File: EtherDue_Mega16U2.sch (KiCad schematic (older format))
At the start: 26 parts, among them IC501 ATMEGA16U2, P501 USB_5PIN_SHELL, U501 74LVC1G125, X501 12MHz KX-7 20pF

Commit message: Remove 74LVC1G125 buffer used for level translation on 16U2 TX pin, replace with resistor divider
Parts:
- removed C504: 100nF, symbol C
- removed U501: 74LVC1G125, symbol 74LVC1G125
- added R509: 1K5, symbol R
- added R510: 2K7, symbol R
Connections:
- net labels removed: +3.3V
- wire segments 106 -> 101

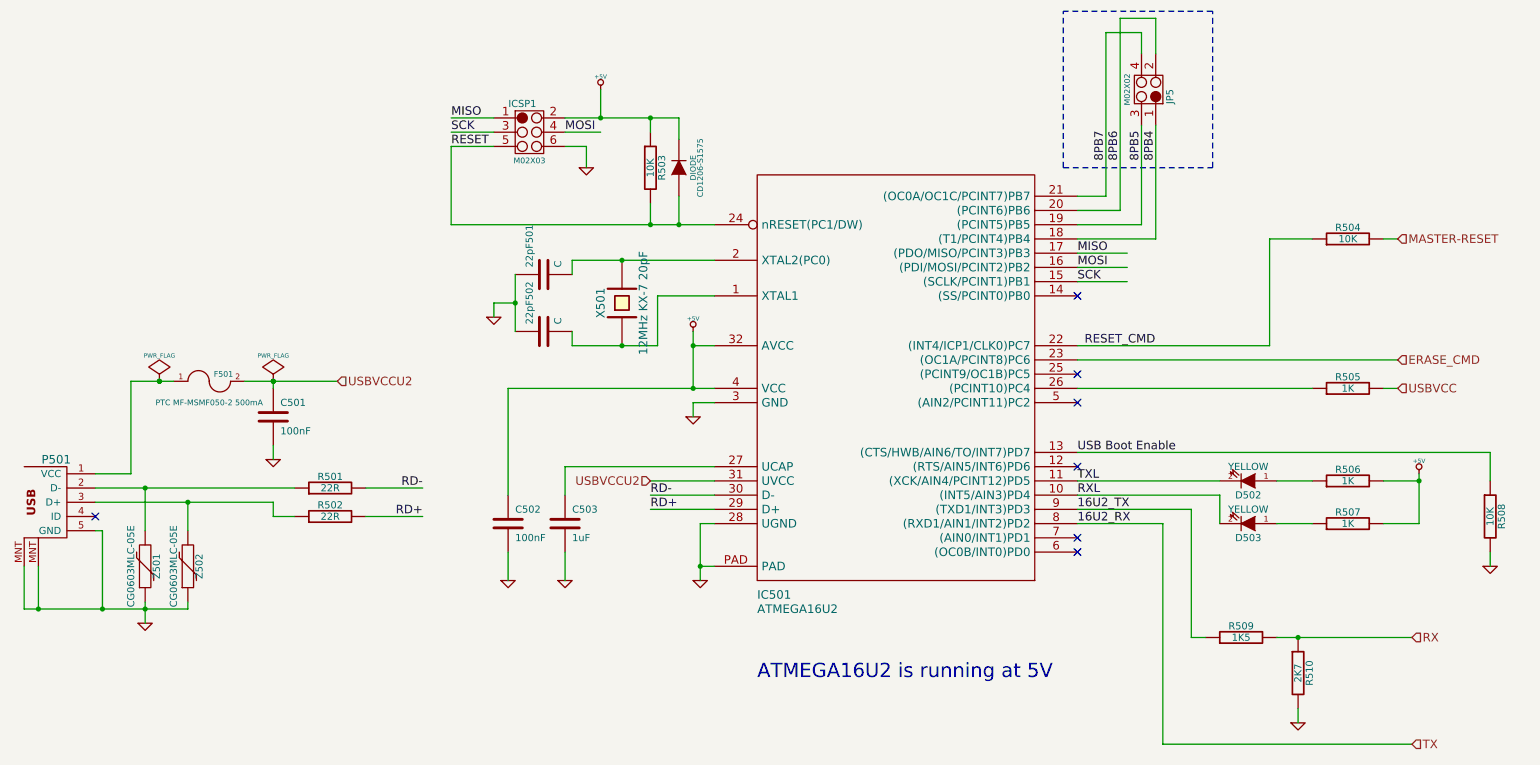
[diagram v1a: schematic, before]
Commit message: Add W5100 Ethernet components
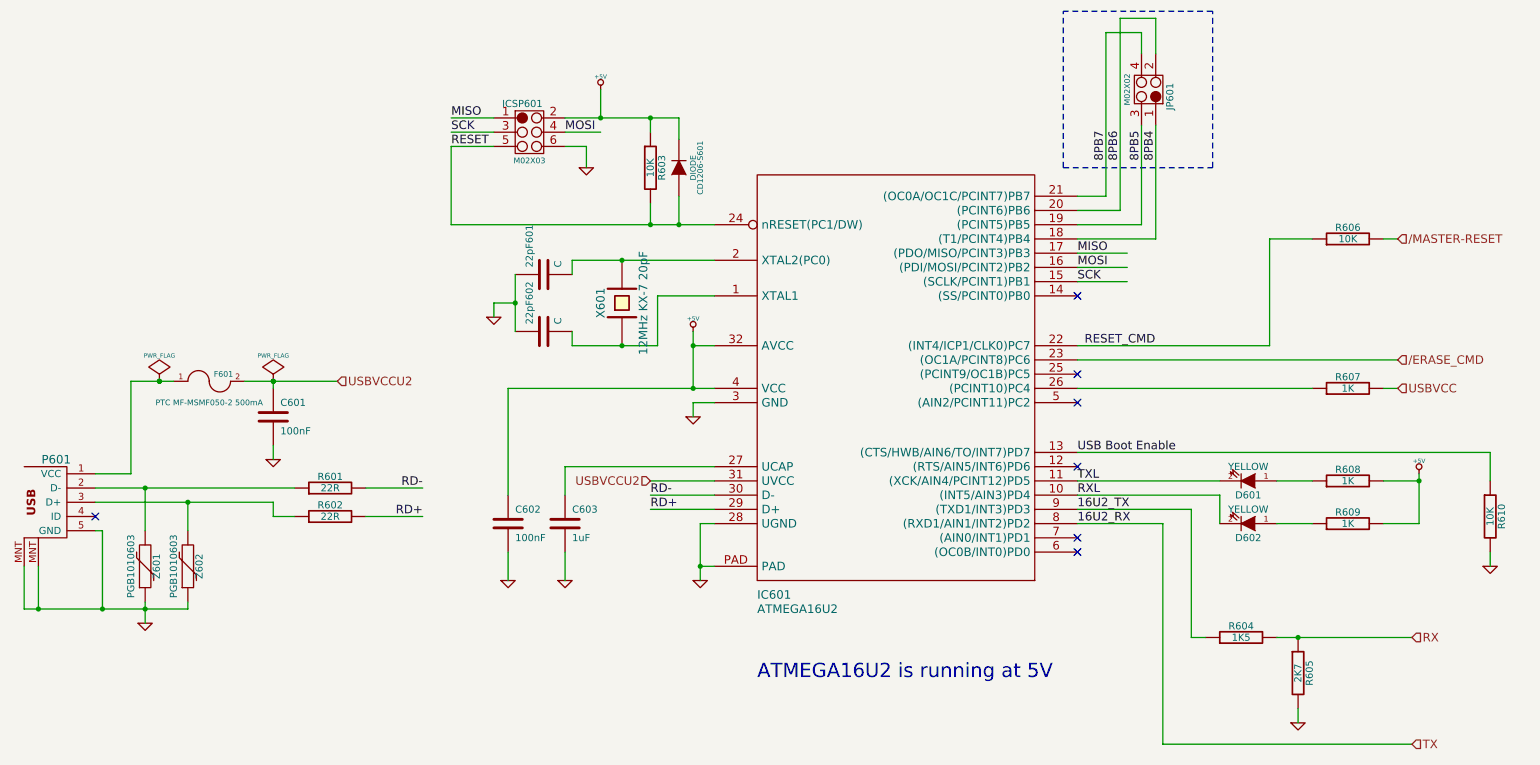
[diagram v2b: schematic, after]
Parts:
- Z601: renamed from Z501; value CG0603MLC-05E -> PGB1010603
- Z602: renamed from Z502; value CG0603MLC-05E -> PGB1010603
- renumbered 22pF501 to 22pF601, 22pF502 to 22pF602, C501 to C601, C502 to C602, C503 to C603, CD1206-S1575 to CD1206-S601, D502 to D601, D503 to D602, F501 to F601, IC501 to IC601, ICSP1 to ICSP601, JP5 to JP601, P501 to P601, R501 to R601, R502 to R602, R503 to R603, R509 to R604, R510 to R605, R504 to R606, R505 to R607, R506 to R608, R507 to R609, R508 to R610, X501 to X601
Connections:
- net labels added: /ERASE_CMD, /MASTER-RESET
- net labels removed: ERASE_CMD, MASTER-RESET
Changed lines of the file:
@@
-EESchema Schematic File Version 2  date Wed 10 Apr 2013 15:09:30 EST
+EESchema Schematic File Version 2  date Thu 11 Apr 2013 15:03:05 EST
 LIBS:power
 LIBS:device
@@
 $Descr A4 11700 8267
 encoding utf-8
-Sheet 5 5
+Sheet 6 6
 Title ""
-Date "10 apr 2013"
+Date "11 apr 2013"
 Rev ""
 Comp ""
@@
 	9650 5800 9650 5900
 $Comp
-L GND #PWR511
+L GND #PWR092
 U 1 1 5164F3D5
 P 9650 5900
-F 0 "#PWR511" H 9650 5900 30  0001 C CNN
+F 0 "#PWR092" H 9650 5900 30  0001 C CNN
 F 1 "GND" H 9650 5830 30  0001 C CNN
 	1    9650 5900
@@
 $EndComp
 $Comp
-L R R510
+L R R605
 U 1 1 5164F3AD
 P 9650 5550
-F 0 "R510" V 9730 5550 50  0000 C CNN
+F 0 "R605" V 9730 5550 50  0000 C CNN
 F 1 "2K7" V 9650 5550 50  0000 C CNN
 	1    9650 5550
@@
 $EndComp
 $Comp
-L R R509
+L R R604
 U 1 1 5164F3A2
 P 9250 5300
-F 0 "R509" V 9330 5300 50  0000 C CNN
+F 0 "R604" V 9330 5300 50  0000 C CNN
 F 1 "1K5" V 9250 5300 50  0000 C CNN
 	1    9250 5300
@@
 $EndComp
 $Comp
-L PWR_FLAG #FLG502
+L PWR_FLAG #FLG093
 U 1 1 5163B502
 P 2450 3500
-F 0 "#FLG502" H 2450 3595 30  0001 C CNN
+F 0 "#FLG093" H 2450 3595 30  0001 C CNN
 F 1 "PWR_FLAG" H 2450 3680 30  0000 C CNN
 	1    2450 3500
@@
 $EndComp
 $Comp
-L PWR_FLAG #FLG501
+L PWR_FLAG #FLG094
 U 1 1 5163B4F2
 P 1650 3500
-F 0 "#FLG501" H 1650 3595 30  0001 C CNN
+F 0 "#FLG094" H 1650 3595 30  0001 C CNN
 F 1 "PWR_FLAG" H 1650 3680 30  0000 C CNN
 	1    1650 3500
@@
 USBVCC
 Text HLabel 10350 3350 2    60   Input ~ 0
-ERASE_CMD
+/ERASE_CMD
 Text HLabel 10350 2500 2    60   Input ~ 0
-MASTER-RESET
+/MASTER-RESET
 Text HLabel 5100 4200 0    60   Input ~ 0
 USBVCCU2
@@
 TXL
 $Comp
-L +5V #PWR512
+L +5V #PWR095
 U 1 1 515BD66E
 P 10500 4150
-F 0 "#PWR512" H 10500 4240 20  0001 C CNN
+F 0 "#PWR095" H 10500 4240 20  0001 C CNN
 F 1 "+5V" H 10500 4240 30  0000 C CNN
 	1    10500 4150
@@
 $EndComp
 $Comp
-L R R506
+L R R608
 U 1 1 515BD664
 P 10000 4200
-F 0 "R506" V 10080 4200 50  0000 C CNN
+F 0 "R608" V 10080 4200 50  0000 C CNN
 F 1 "1K" V 10000 4200 50  0000 C CNN
 	1    10000 4200
@@
 $EndComp
 $Comp
-L R R507
+L R R609
 U 1 1 515BD654
 P 10000 4500
-F 0 "R507" V 10080 4500 50  0000 C CNN
+F 0 "R609" V 10080 4500 50  0000 C CNN
 F 1 "1K" V 10000 4500 50  0000 C CNN
 	1    10000 4500
@@
 $EndComp
 $Comp
-L LED D503
+L LED D602
 U 1 1 515BD64B
 P 9300 4500
-F 0 "D503" H 9300 4600 50  0000 C CNN
+F 0 "D602" H 9300 4600 50  0000 C CNN
 F 1 "YELLOW" H 9300 4400 50  0000 C CNN
 	1    9300 4500
@@
 $EndComp
 $Comp
-L LED D502
+L LED D601
 U 1 1 515BD62A
 P 9300 4200
-F 0 "D502" H 9300 4300 50  0000 C CNN
+F 0 "D601" H 9300 4300 50  0000 C CNN
 F 1 "YELLOW" H 9300 4100 50  0000 C CNN
 	1    9300 4200
@@
 NoConn ~ 8100 4100
 $Comp
-L GND #PWR513
+L GND #PWR096
 U 1 1 515BD60A
 P 11000 4800
-F 0 "#PWR513" H 11000 4800 30  0001 C CNN
+F 0 "#PWR096" H 11000 4800 30  0001 C CNN
 F 1 "GND" H 11000 4730 30  0001 C CNN
 	1    11000 4800
@@
 $EndComp
 $Comp
-L R R508
+L R R610
 U 1 1 515BD5FC
 P 11000 4450
-F 0 "R508" V 11080 4450 50  0000 C CNN
+F 0 "R610" V 11080 4450 50  0000 C CNN
 F 1 "10K" V 11000 4450 50  0000 C CNN
 	1    11000 4450
@@
 NoConn ~ 8100 3650
 $Comp
-L R R505
+L R R607
 U 1 1 515BD5C8
 P 10000 3550
-F 0 "R505" V 10080 3550 50  0000 C CNN
+F 0 "R607" V 10080 3550 50  0000 C CNN
 F 1 "1K" V 10000 3550 50  0000 C CNN
 	1    10000 3550
@@
 RESET_CMD
 $Comp
-L R R504
+L R R606
 U 1 1 515BD538
 P 10000 2500
-F 0 "R504" V 10080 2500 50  0000 C CNN
+F 0 "R606" V 10080 2500 50  0000 C CNN
 F 1 "10K" V 10000 2500 50  0000 C CNN
 	1    10000 2500
@@
 RD-
 $Comp
-L R R502
+L R R602
 U 1 1 515BD4B0
 P 2850 4450
-F 0 "R502" V 2930 4450 50  0000 C CNN
+F 0 "R602" V 2930 4450 50  0000 C CNN
 F 1 "22R" V 2850 4450 50  0000 C CNN
 	1    2850 4450
@@
 $EndComp
 $Comp
-L R R501
+L R R601
 U 1 1 515BD4A7
 P 2850 4250
-F 0 "R501" V 2930 4250 50  0000 C CNN
+F 0 "R601" V 2930 4250 50  0000 C CNN
 F 1 "22R" V 2850 4250 50  0000 C CNN
 	1    2850 4250
@@
 NoConn ~ 1200 4450
 $Comp
-L VR Z502
+L VR Z602
 U 1 1 515BD423
 P 1850 4800
-F 0 "Z502" V 1930 4800 50  0000 C CNN
-F 1 "CG0603MLC-05E" V 1750 4800 50  0000 C CNN
+F 0 "Z602" V 1930 4800 50  0000 C CNN
+F 1 "PGB1010603" V 1750 4800 50  0000 C CNN
 	1    1850 4800
 	1    0    0    1
 $EndComp
 $Comp
-L VR Z501
+L VR Z601
 U 1 1 515BD3FE
 P 1550 4800
-F 0 "Z501" V 1630 4800 50  0000 C CNN
-F 1 "CG0603MLC-05E" V 1450 4800 50  0000 C CNN
+F 0 "Z601" V 1630 4800 50  0000 C CNN
+F 1 "PGB1010603" V 1450 4800 50  0000 C CNN
 	1    1550 4800
 	1    0    0    1
 $EndComp
 $Comp
-L GND #PWR501
+L GND #PWR097
 U 1 1 515BD32A
 P 1550 5200
-F 0 "#PWR501" H 1550 5200 30  0001 C CNN
+F 0 "#PWR097" H 1550 5200 30  0001 C CNN
 F 1 "GND" H 1550 5130 30  0001 C CNN
 	1    1550 5200
@@
 $EndComp
 $Comp
-L GND #PWR502
+L GND #PWR098
 U 1 1 515BD31D
 P 2450 4050
-F 0 "#PWR502" H 2450 4050 30  0001 C CNN
+F 0 "#PWR098" H 2450 4050 30  0001 C CNN
 F 1 "GND" H 2450 3980 30  0001 C CNN
 	1    2450 4050
@@
 $EndComp
 $Comp
-L C C501
+L C C601
 U 1 1 515BD2FA
 P 2450 3750
-F 0 "C501" H 2500 3850 50  0000 L CNN
+F 0 "C601" H 2500 3850 50  0000 L CNN
 F 1 "100nF" H 2500 3650 50  0000 L CNN
 	1    2450 3750
@@
 $EndComp
 $Comp
-L FUSE F501
+L FUSE F601
 U 1 1 515BD2D5
 P 2000 3500
-F 0 "F501" H 2100 3550 40  0000 C CNN
+F 0 "F601" H 2100 3550 40  0000 C CNN
 F 1 "PTC MF-MSMF050-2 500mA" H 2000 3350 40  0000 C CNN
 	1    2000 3500
@@
 $EndComp
 $Comp
-L USB_5PIN_SHELL P501
+L USB_5PIN_SHELL P601
 U 1 1 515BD282
 P 1000 4300
-F 0 "P501" H 925 4550 60  0000 C CNN
+F 0 "P601" H 925 4550 60  0000 C CNN
 F 1 "USB_5PIN_SHELL" H 1200 3950 60  0001 C CNN
 	1    1000 4300
@@
 RD-
 $Comp
-L GND #PWR510
+L GND #PWR099
 U 1 1 515BD1F5
 P 5450 4900
-F 0 "#PWR510" H 5450 4900 30  0001 C CNN
+F 0 "#PWR099" H 5450 4900 30  0001 C CNN
 F 1 "GND" H 5450 4830 30  0001 C CNN
 	1    5450 4900
@@
 $EndComp
 $Comp
-L GND #PWR509
+L GND #PWR0100
 U 1 1 515BD1F3
 P 5400 3750
-F 0 "#PWR509" H 5400 3750 30  0001 C CNN
+F 0 "#PWR0100" H 5400 3750 30  0001 C CNN
 F 1 "GND" H 5400 3680 30  0001 C CNN
 	1    5400 3750
@@
 $EndComp
 $Comp
-L GND #PWR505
+L GND #PWR0101
 U 1 1 515BD19C
 P 4500 4900
-F 0 "#PWR505" H 4500 4900 30  0001 C CNN
+F 0 "#PWR0101" H 4500 4900 30  0001 C CNN
 F 1 "GND" H 4500 4830 30  0001 C CNN
 	1    4500 4900
@@
 $EndComp
 $Comp
-L GND #PWR504
+L GND #PWR0102
 U 1 1 515BD198
 P 4100 4900
-F 0 "#PWR504" H 4100 4900 30  0001 C CNN
+F 0 "#PWR0102" H 4100 4900 30  0001 C CNN
 F 1 "GND" H 4100 4830 30  0001 C CNN
 	1    4100 4900
@@
 $EndComp
 $Comp
-L C C503
+L C C603
 U 1 1 515BD169
 P 4500 4500
-F 0 "C503" H 4550 4600 50  0000 L CNN
+F 0 "C603" H 4550 4600 50  0000 L CNN
 F 1 "1uF" H 4550 4400 50  0000 L CNN
 	1    4500 4500
@@
 $EndComp
 $Comp
-L C C502
+L C C602
 U 1 1 515BD15F
 P 4100 4500
-F 0 "C502" H 4150 4600 50  0000 L CNN
+F 0 "C602" H 4150 4600 50  0000 L CNN
 F 1 "100nF" H 4150 4400 50  0000 L CNN
 	1    4100 4500
@@
 $EndComp
 $Comp
-L +5V #PWR508
+L +5V #PWR0103
 U 1 1 515BD14E
 P 5400 3150
-F 0 "#PWR508" H 5400 3240 20  0001 C CNN
+F 0 "#PWR0103" H 5400 3240 20  0001 C CNN
 F 1 "+5V" H 5400 3240 30  0000 C CNN
 	1    5400 3150
@@
 $EndComp
 $Comp
-L GND #PWR503
+L GND #PWR0104
 U 1 1 515BCFAA
 P 4000 3050
-F 0 "#PWR503" H 4000 3050 30  0001 C CNN
+F 0 "#PWR0104" H 4000 3050 30  0001 C CNN
 F 1 "GND" H 4000 2980 30  0001 C CNN
 	1    4000 3050
@@
 $EndComp
 $Comp
-L C 22pF502
+L C 22pF602
 U 1 1 515BCF9F
 P 4350 3150
-F 0 "22pF502" H 4400 3250 50  0000 L CNN
+F 0 "22pF602" H 4400 3250 50  0000 L CNN
 F 1 "C" H 4400 3050 50  0000 L CNN
 	1    4350 3150
@@
 $EndComp
 $Comp
-L C 22pF501
+L C 22pF601
 U 1 1 515BCF8C
 P 4350 2750
-F 0 "22pF501" H 4400 2850 50  0000 L CNN
+F 0 "22pF601" H 4400 2850 50  0000 L CNN
 F 1 "C" H 4400 2650 50  0000 L CNN
 	1    4350 2750
@@
 $EndComp
 $Comp
-L CRYSTAL X501
+L CRYSTAL X601
 U 1 1 515BCF7E
 P 4900 2950
-F 0 "X501" H 4900 3100 60  0000 C CNN
+F 0 "X601" H 4900 3100 60  0000 C CNN
 F 1 "12MHz KX-7 20pF" H 4900 2800 60  0000 C CNN
 	1    4900 2950
@@
 8PB7
 $Comp
-L M02X02 JP5
+L M02X02 JP601
 U 1 1 515BCEC1
 P 8650 1400
-F 0 "JP5" H 8550 1500 50  0000 C CNN
+F 0 "JP601" H 8550 1500 50  0000 C CNN
 F 1 "M02X02" H 8600 1200 40  0000 C CNN
 	1    8650 1400
@@
 MISO
 $Comp
-L DIODE CD1206-S1575
+L DIODE CD1206-S601
 U 1 1 515BCE47
 P 5300 2000
-F 0 "CD1206-S1575" H 5300 1850 40  0000 C CNN
+F 0 "CD1206-S601" H 5300 1850 40  0000 C CNN
 F 1 "DIODE" H 5300 1900 40  0000 C CNN
 	1    5300 2000
@@
 $EndComp
 $Comp
-L +5V #PWR507
+L +5V #PWR0105
 U 1 1 515BCDF5
 P 4750 1450
-F 0 "#PWR507" H 4750 1540 20  0001 C CNN
+F 0 "#PWR0105" H 4750 1540 20  0001 C CNN
 F 1 "+5V" H 4750 1540 30  0000 C CNN
 	1    4750 1450
@@
 $EndComp
 $Comp
-L R R503
+L R R603
 U 1 1 515BCDE2
 P 5100 2000
-F 0 "R503" V 5180 2000 50  0000 C CNN
+F 0 "R603" V 5180 2000 50  0000 C CNN
 F 1 "10K" V 5100 2000 50  0000 C CNN
 	1    5100 2000
@@
 $EndComp
 $Comp
-L GND #PWR506
+L GND #PWR0106
 U 1 1 515BCDA9
 P 4650 2000
-F 0 "#PWR506" H 4650 2000 30  0001 C CNN
+F 0 "#PWR0106" H 4650 2000 30  0001 C CNN
 F 1 "GND" H 4650 1930 30  0001 C CNN
 	1    4650 2000
@@
 MISO
 $Comp
-L M02X03 ICSP1
+L M02X03 ICSP601
 U 1 1 515BCD62
 P 4300 1650
-F 0 "ICSP1" H 4200 1750 50  0000 C CNN
+F 0 "ICSP601" H 4200 1750 50  0000 C CNN
 F 1 "M02X03" H 4250 1350 40  0000 C CNN
 	1    4300 1650
@@
 $EndComp
 $Comp
-L ATMEGA16U2 IC501
+L ATMEGA16U2 IC601
 U 1 1 515BCD3F
 P 6900 3250
-F 0 "IC501" H 5850 1500 60  0000 L CNN
+F 0 "IC601" H 5850 1500 60  0000 L CNN
 F 1 "ATMEGA16U2" H 5850 1400 60  0000 L CNN
 	1    6900 3250
